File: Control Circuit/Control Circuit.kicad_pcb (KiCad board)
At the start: 2 copper layers, 120 x 118.6 mm, 4 parts, among them U1 Adafruit DPS310, U3 Adafruit BNO085

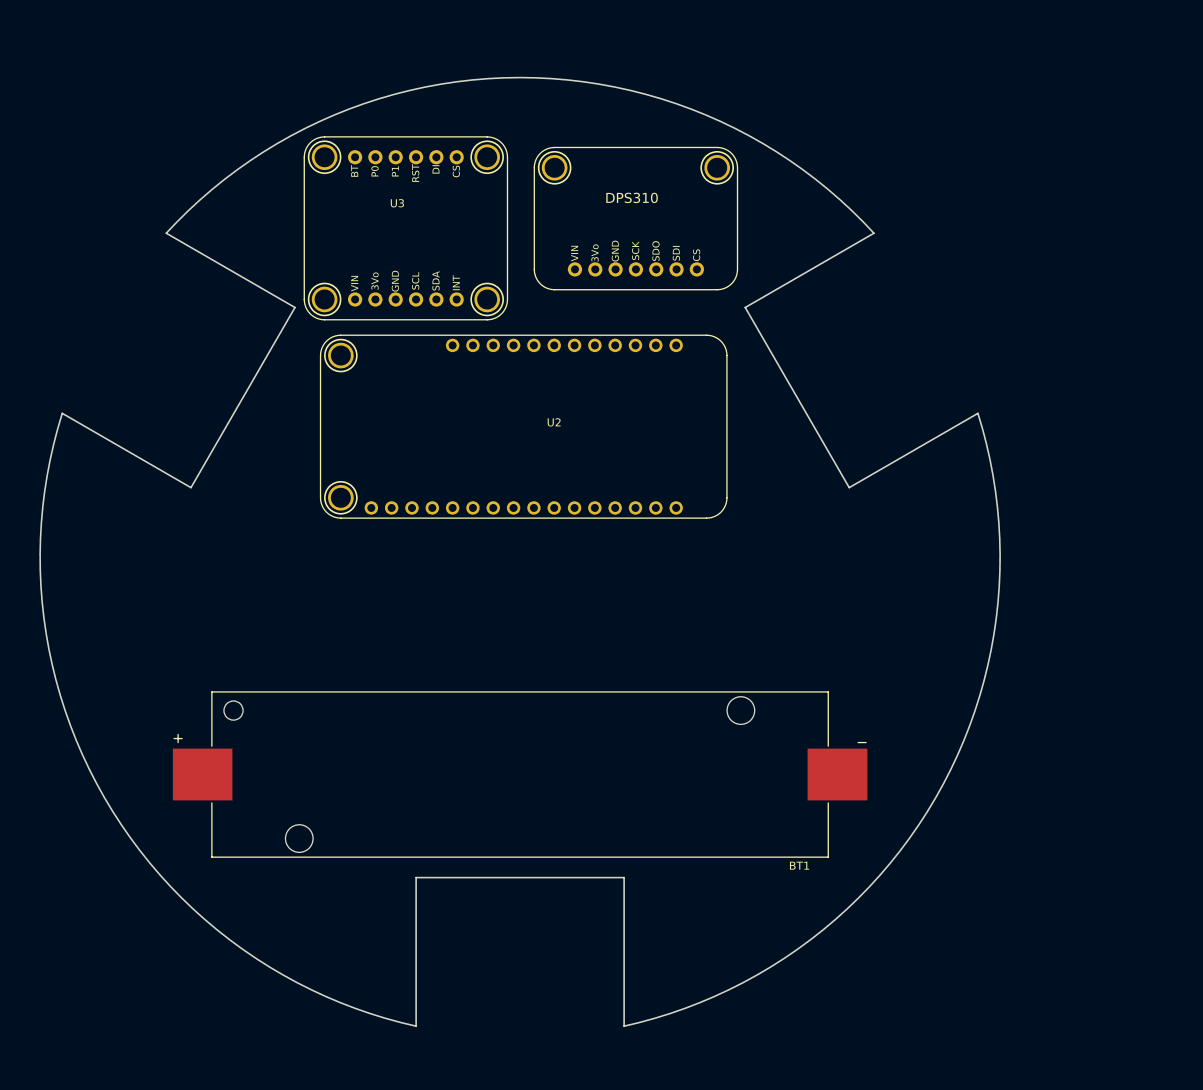
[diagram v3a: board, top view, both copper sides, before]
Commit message: fixed board outline and added mounting holes
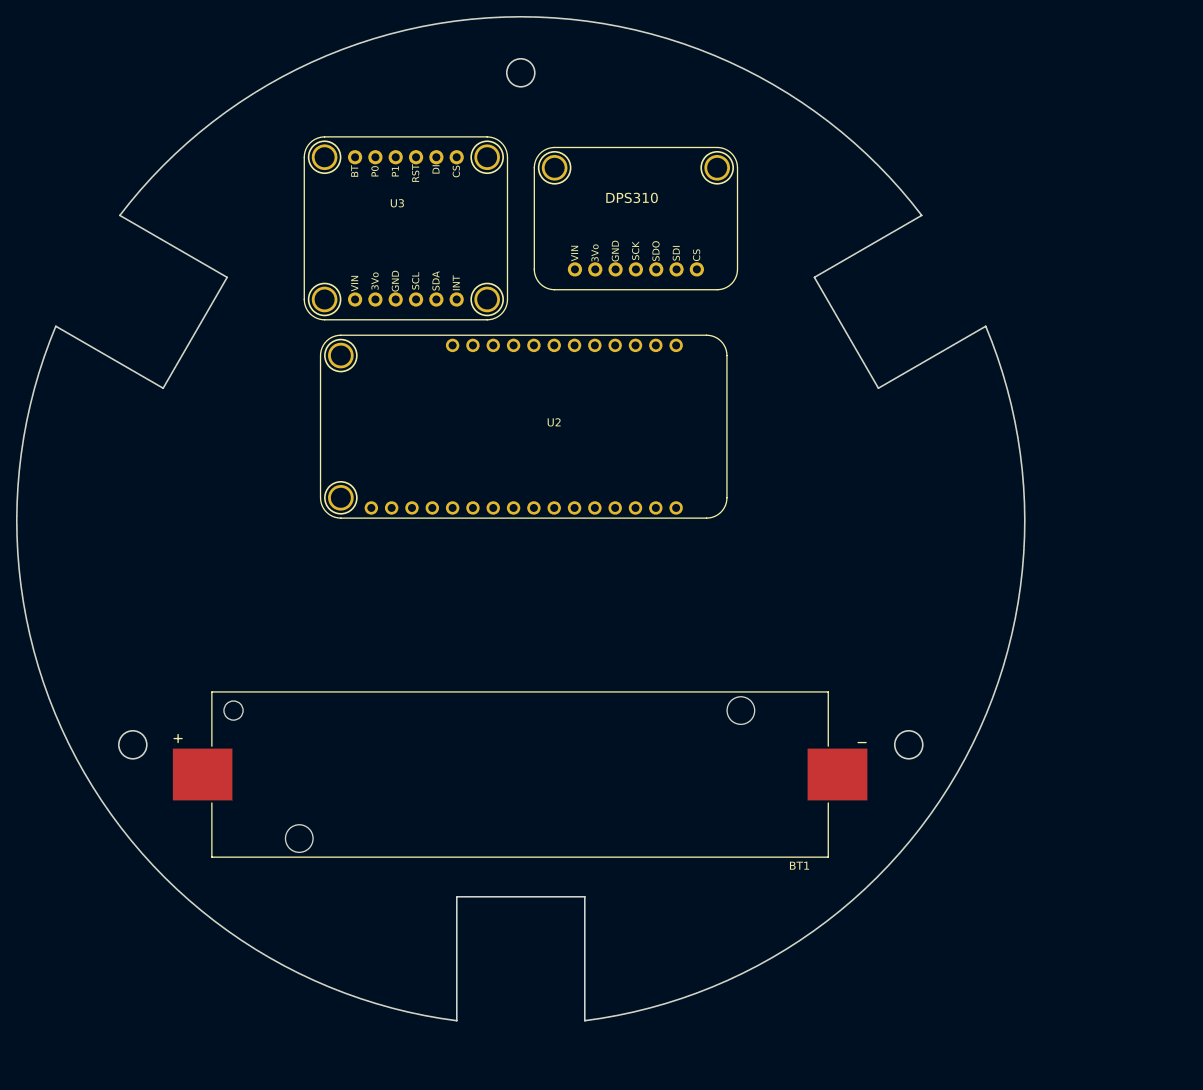
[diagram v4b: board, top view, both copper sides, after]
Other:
- board size 120 x 118.6 mm -> 126 x 125.5 mm
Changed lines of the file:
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@@
     )
   )
-  (gr_line (start 140.768388 68.214299) (end 153.768388 90.73096)
+  (gr_line (start 120.712805 157.363999) (end 120.712805 141.874001)
     (stroke (width 0.2) (type solid)) (layer "Edge.Cuts"))
-  (gr_line (start 125.627371 158.047369) (end 125.627371 139.472631)
+  (gr_line (start 104.712805 141.874001) (end 104.712805 157.363999)
     (stroke (width 0.2) (type solid)) (layer "Edge.Cuts"))
-  (gr_line (start 125.627371 139.472631) (end 99.627371 139.472631)
+  (gr_line (start 162.830732 56.700797) (end 149.416 64.445796)
     (stroke (width 0.2) (type solid)) (layer "Edge.Cuts"))
-  (gr_line (start 156.854583 58.92693) (end 140.768388 68.214299)
+  (gr_line (start 149.416 64.445796) (end 157.416 78.302203)
     (stroke (width 0.2) (type solid)) (layer "Edge.Cuts"))
-  (gr_line (start 84.486354 68.214299) (end 68.400159 58.92693)
+  (gr_circle (center 64.215382 122.874) (end 64.215382 124.624)
+    (stroke (width 0.2) (type solid)) (fill none) (layer "Edge.Cuts"))
+  (gr_circle (center 112.712805 38.874) (end 112.712805 40.624)
+    (stroke (width 0.2) (type solid)) (fill none) (layer "Edge.Cuts"))
+  (gr_arc (start 170.830732 70.557204) (mid 167.272405 126.374) (end 120.712805 157.363999)
     (stroke (width 0.2) (type solid)) (layer "Edge.Cuts"))
-  (gr_arc (start 169.854583 81.443591) (mid 164.588895 129.47263) (end 125.627371 158.047369)
+  (gr_line (start 68.00961 78.302203) (end 76.00961 64.445796)
     (stroke (width 0.2) (type solid)) (layer "Edge.Cuts"))
-  (gr_line (start 71.486354 90.73096) (end 84.486354 68.214299)
+  (gr_arc (start 104.712805 157.363999) (mid 58.153205 126.374) (end 54.594878 70.557204)
     (stroke (width 0.2) (type solid)) (layer "Edge.Cuts"))
-  (gr_arc (start 99.627371 158.047369) (mid 60.665846 129.47263) (end 55.400159 81.443591)
+  (gr_circle (center 161.210228 122.874) (end 161.210228 124.624)
+    (stroke (width 0.2) (type solid)) (fill none) (layer "Edge.Cuts"))
+  (gr_line (start 54.594878 70.557204) (end 68.00961 78.302203)
     (stroke (width 0.2) (type solid)) (layer "Edge.Cuts"))
-  (gr_arc (start 68.400159 58.92693) (mid 112.627371 39.472629) (end 156.854583 58.92693)
+  (gr_line (start 120.712805 141.874001) (end 104.712805 141.874001)
     (stroke (width 0.2) (type solid)) (layer "Edge.Cuts"))
-  (gr_line (start 55.400159 81.443591) (end 71.486354 90.73096)
+  (gr_line (start 157.416 78.302203) (end 170.830732 70.557204)
     (stroke (width 0.2) (type solid)) (layer "Edge.Cuts"))
-  (gr_line (start 99.627371 139.472631) (end 99.627371 158.047369)
+  (gr_line (start 76.00961 64.445796) (end 62.594878 56.700797)
     (stroke (width 0.2) (type solid)) (layer "Edge.Cuts"))
-  (gr_line (start 153.768388 90.73096) (end 169.854583 81.443591)
+  (gr_arc (start 62.594878 56.700797) (mid 112.712805 31.874) (end 162.830732 56.700797)
     (stroke (width 0.2) (type solid)) (layer "Edge.Cuts"))
-  (group "" (id d9ff58da-d626-4267-b94a-bc169973c5e5)
+  (group "" (id 324d6864-1f71-4817-a239-f9279aa4a756)
     (members
-      03e5a22f-747a-4755-b2d9-5b0fd53b9463
-      1bf3ae57-108e-432e-935b-dc585a51e9f2
-      1cff9b36-c665-4a7f-8d07-4fa604743f36
-      3126e0ea-1537-4ed2-8ee2-12426cb289b1
-      41f21fc9-91e7-424a-b463-4139455cccdd
-      b1c2d789-4e2b-4df5-a4ae-ac27cbc04bc7
-      baa51c8c-5b4c-489d-906b-d9b7b1bd2978
-      d7bb7529-d266-475d-9266-311995f215a5
-      df1be2f9-9ed0-401a-a2f8-5f0bf1c350b6
-      e0b4e479-4ccb-408d-ad39-4ea0b5519bc5
-      ea232489-3607-4806-962b-fc4ea7b62cc3
-      f7ef9afd-121d-4120-856b-5c997b0fda9b
+      09b8c23a-1f51-471f-a565-35cede87b007
+      166a0128-0c36-41f1-8b13-ecc424346e09
+      2ce54812-1458-4f63-9cd5-9c4ea2b928c7
+      408764ba-3130-4400-bb85-3a224ef40bc6
+      47839536-f448-4306-afd0-269b7f953c80
+      5c310ec8-37a9-435e-b528-3f39bd97f642
+      623a9802-1b4d-4df5-8d45-780ff481b41d
+      65b451d2-6755-4079-a72e-6c761de1e828
+      7e5c99e4-9ee6-4538-ac20-69fd0baad7b4
+      94c514a5-5a45-4bf1-a2bb-0f660a451db5
+      be93f8ce-a520-4d6d-8ea7-5687b0ea8049
+      d4da4b82-c26a-474e-8f0e-cf65430ccbda
+      d9ef36b6-9cc1-4cf3-8450-1d7c94a52837
+      ee949416-f8c1-4a6e-8aad-446d1e79eced
+      f076d7ab-7db0-404b-a4b5-2c81582e7668
     )
   )

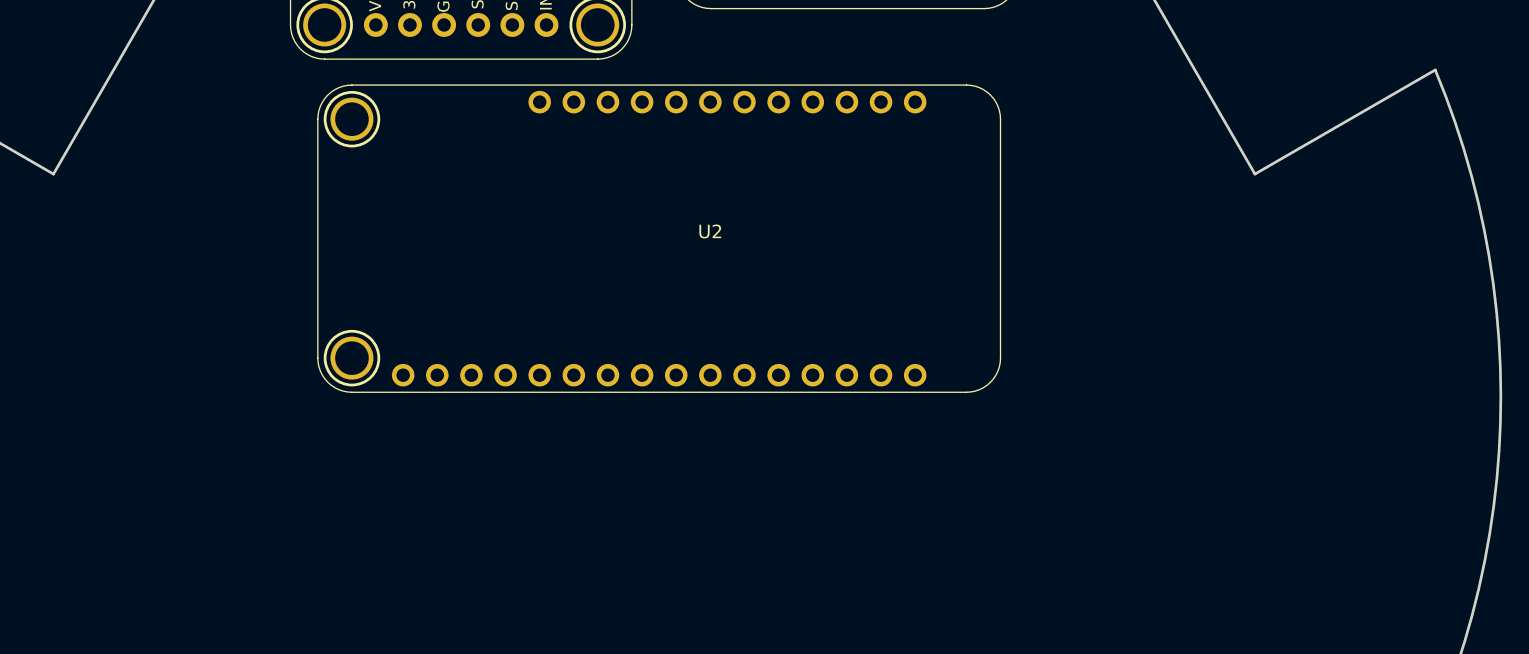
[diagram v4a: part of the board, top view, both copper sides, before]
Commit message: added power conversion pcb
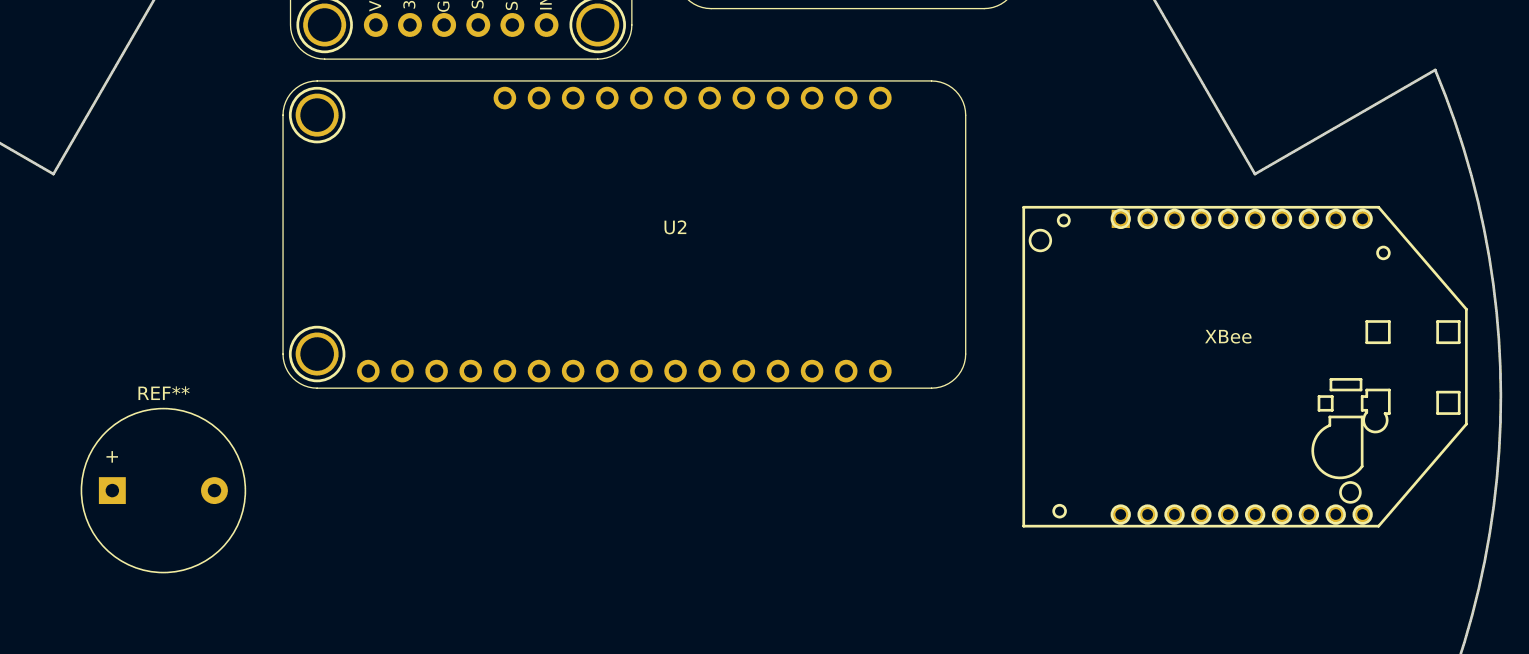
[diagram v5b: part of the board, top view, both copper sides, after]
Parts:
- added REF**: Buzzer_12x9.5RM7.6, Buzzer_Beeper:Buzzer_12x9.5RM7.6, F.Cu at (72.4, 101.9)
- added XBee: Digi XBee, Digi XBee:Digi XBee, F.Cu at (155.4, 90.9)
- moved U2 2.61 mm to (114.3, 82.8)

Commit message: added symbol and foot print for boost converter
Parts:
- added U4: TPS61087, Boost Converter:TPS61087 Breakout, F.Cu at (107.5, 104.2)
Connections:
- BT1 pad N: unconnected-(BT1-PadN) -> Net-(BT1-PadN)
- BT1 pad P: unconnected-(BT1-PadP) -> Net-(U4-VIN)
